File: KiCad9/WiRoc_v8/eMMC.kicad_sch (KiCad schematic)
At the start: 10 parts, among them U14 KLM8G1WEPD-B031

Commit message: etc
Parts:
- C33, C34, C86: LCSC Part # (none) -> C52923; Manufacturer (none) -> Samsung Electro-Mechanics; ManufacturerPartNumber (none) -> CL05A105KA5NQNC
- R26: LCSC Part # (none) -> C25804; Manufacturer (none) -> Uniroyal Elec; ManufacturerPartNumber (none) -> 0603WAF1002T5E
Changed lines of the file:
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@@
 			)
 		)
-		(property "Datasheet" "~"
+		(property "Datasheet" "https://jlcpcb.com/api/file/downloadByFileSystemAccessId/8579707174974914560"
 			(at 213.36 78.74 0)
 			(effects
@@
 		)
 		(property "Description" ""
+			(at 213.36 78.74 0)
+			(effects
+				(font
+					(size 1.27 1.27)
+				)
+				(hide yes)
+			)
+		)
+		(property "LCSC Part #" "C52923"
+			(at 213.36 78.74 0)
+			(effects
+				(font
+					(size 1.27 1.27)
+				)
+				(hide yes)
+			)
+		)
+		(property "Manufacturer" "Samsung Electro-Mechanics"
+			(at 213.36 78.74 0)
+			(effects
+				(font
+					(size 1.27 1.27)
+				)
+				(hide yes)
+			)
+		)
+		(property "ManufacturerPartNumber" "CL05A105KA5NQNC"
 			(at 213.36 78.74 0)
 			(effects
@@
 			)
 		)
-		(property "Datasheet" "~"
+		(property "Datasheet" "https://jlcpcb.com/api/file/downloadByFileSystemAccessId/8579707174974914560"
 			(at 36.83 153.67 0)
 			(effects
@@
 		)
 		(property "Description" ""
+			(at 36.83 153.67 0)
+			(effects
+				(font
+					(size 1.27 1.27)
+				)
+				(hide yes)
+			)
+		)
+		(property "LCSC Part #" "C52923"
+			(at 36.83 153.67 0)
+			(effects
+				(font
+					(size 1.27 1.27)
+				)
+				(hide yes)
+			)
+		)
+		(property "Manufacturer" "Samsung Electro-Mechanics"
+			(at 36.83 153.67 0)
+			(effects
+				(font
+					(size 1.27 1.27)
+				)
+				(hide yes)
+			)
+		)
+		(property "ManufacturerPartNumber" "CL05A105KA5NQNC"
 			(at 36.83 153.67 0)
 			(effects
@@
 			)
 		)
-		(property "Datasheet" "~"
+		(property "Datasheet" "https://jlcpcb.com/api/file/downloadByFileSystemAccessId/8579707174974914560"
 			(at 213.36 54.61 0)
 			(effects
@@
 		)
 		(property "Description" ""
+			(at 213.36 54.61 0)
+			(effects
+				(font
+					(size 1.27 1.27)
+				)
+				(hide yes)
+			)
+		)
+		(property "LCSC Part #" "C52923"
+			(at 213.36 54.61 0)
+			(effects
+				(font
+					(size 1.27 1.27)
+				)
+				(hide yes)
+			)
+		)
+		(property "Manufacturer" "Samsung Electro-Mechanics"
+			(at 213.36 54.61 0)
+			(effects
+				(font
+					(size 1.27 1.27)
+				)
+				(hide yes)
+			)
+		)
+		(property "ManufacturerPartNumber" "CL05A105KA5NQNC"
 			(at 213.36 54.61 0)
 			(effects
@@
 			(at 39.37 45.72 0)
 			(effects
+				(font
+					(size 1.27 1.27)
+				)
+				(hide yes)
+			)
+		)
+		(property "LCSC Part #" "C25804"
+			(at 39.37 45.72 0)
+			(effects
+				(font
+					(size 1.27 1.27)
+				)
+				(hide yes)
+			)
+		)
+		(property "Manufacturer" "Uniroyal Elec"
+			(at 39.37 45.72 0)
+			(effects
+				(font
+					(size 1.27 1.27)
+				)
+				(hide yes)
+			)
+		)
+		(property "ManufacturerPartNumber" "0603WAF1002T5E"
+			(at 39.37 45.72 0)
+			(effects

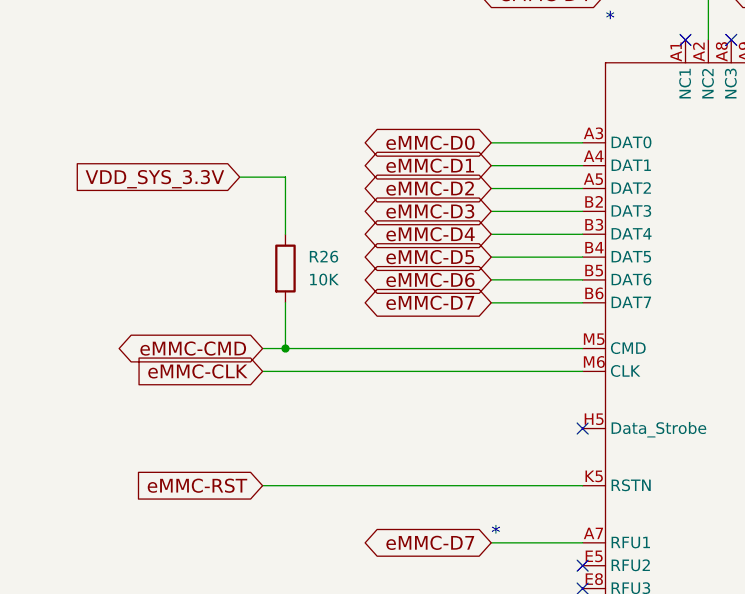
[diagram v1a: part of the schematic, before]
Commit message: more routing of WiRoc_v8, upgraded USBConnectorPlate to v9 and with ferrit beads, added an ESPHosted testboard
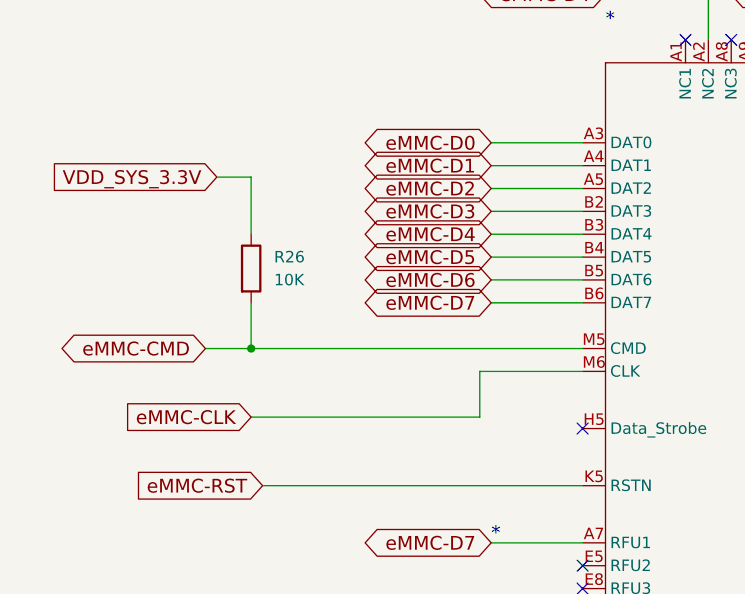
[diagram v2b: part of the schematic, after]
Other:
- moved on the sheet: R26
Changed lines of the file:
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@@
 	)
 	(junction
+		(at 35.56 54.61)
+		(diameter 0)
+		(color 0 0 0 0)
+	)
+	(junction
 		(at 66.04 176.53)
 		(diameter 0)
@@
 	)
 	(junction
-		(at 39.37 54.61)
-		(diameter 0)
-		(color 0 0 0 0)
-	)
-	(junction
 		(at 66.04 168.91)
 		(diameter 0)
@@
 	(wire
 		(pts
-			(xy 59.69 146.05) (xy 72.39 146.05)
+			(xy 60.96 57.15) (xy 72.39 57.15)
 		)
 		(stroke
@@
 	(wire
 		(pts
-			(xy 39.37 54.61) (xy 72.39 54.61)
+			(xy 59.69 146.05) (xy 72.39 146.05)
 		)
 		(stroke
@@
 	(wire
 		(pts
-			(xy 39.37 49.53) (xy 39.37 54.61)
+			(xy 35.56 49.53) (xy 35.56 54.61)
 		)
 		(stroke
@@
 	(wire
 		(pts
-			(xy 34.29 35.56) (xy 39.37 35.56)
+			(xy 31.75 35.56) (xy 35.56 35.56)
 		)
 		(stroke
@@
 	(wire
 		(pts
-			(xy 36.83 57.15) (xy 72.39 57.15)
+			(xy 35.56 62.23) (xy 60.96 62.23)
 		)
 		(stroke
@@
 	(wire
 		(pts
-			(xy 39.37 35.56) (xy 39.37 41.91)
+			(xy 35.56 35.56) (xy 35.56 41.91)
 		)
 		(stroke
@@
 	(wire
 		(pts
-			(xy 36.83 54.61) (xy 39.37 54.61)
+			(xy 30.48 54.61) (xy 35.56 54.61)
 		)
 		(stroke
@@
 	(wire
 		(pts
+			(xy 60.96 62.23) (xy 60.96 57.15)
+		)
+		(stroke
+			(width 0)
+			(type default)
+		)
+	)
+	(wire
+		(pts
 			(xy 63.5 134.62) (xy 72.39 134.62)
 		)
@@
 	(wire
 		(pts
+			(xy 35.56 54.61) (xy 72.39 54.61)
+		)
+		(stroke
+			(width 0)
+			(type default)
+		)
+	)
+	(wire
+		(pts
 			(xy 36.83 149.86) (xy 36.83 146.05)
 		)
@@
 	(global_label "eMMC-CMD"
 		(shape bidirectional)
-		(at 36.83 54.61 180)
+		(at 30.48 54.61 180)
 		(fields_autoplaced yes)
 		(effects
@@
 		)
 		(property "Intersheetrefs" "${INTERSHEET_REFS}"
-			(at 19.8999 54.61 0)
+			(at 13.5499 54.61 0)
 			(effects
 				(font
@@
 	(global_label "eMMC-CLK"
 		(shape input)
-		(at 36.83 57.15 180)
+		(at 35.56 62.23 180)
 		(fields_autoplaced yes)
 		(effects
@@
 		)
 		(property "Intersheetrefs" "${INTERSHEET_REFS}"
-			(at 21.5509 57.15 0)
+			(at 20.2809 62.23 0)
 			(effects
 				(font
@@
 	(global_label "VDD_SYS_3.3V"
 		(shape input)
-		(at 34.29 35.56 180)
+		(at 31.75 35.56 180)
 		(fields_autoplaced yes)
 		(effects
@@
 		)
 		(property "Intersheetrefs" "${INTERSHEET_REFS}"
-			(at 15.6728 35.56 0)
+			(at 13.1328 35.56 0)
 			(effects
 				(font
@@
 		)
 	)
+	(rule_area
+		(polyline
+			(pts
+				(xy 68.58 30.48) (xy 64.77 30.48) (xy 64.77 50.8) (xy 68.58 50.8)
+			)
+			(stroke
+				(width 0)
+				(type dash)
+			)
+			(fill
+				(type none)
+			)
+		)
+	)
+	(netclass_flag ""
+		(length 2.54)
+		(shape round)
+		(at 40.64 54.61 0)
+		(fields_autoplaced yes)
+		(effects
+			(font
+				(size 1.524 1.524)
+			)
+			(justify left bottom)
+		)
+		(property "Netclass" "eMMC-Cmd"
+			(at 41.2699 52.07 0)
+			(effects
+				(font
+					(size 1.27 1.27)
+				)
+				(justify left)
+			)
+		)
+		(property "Component Class" ""
+			(at -121.92 12.7 0)
+			(effects
+				(font
+					(size 1.27 1.27)
+					(italic yes)
+				)
+			)
+		)
+	)
+	(netclass_flag ""
+		(length 2.54)
+		(shape round)
+		(at 66.04 30.48 0)
+		(fields_autoplaced yes)
+		(effects
+			(font
+				(size 1.524 1.524)
+			)
+			(justify left bottom)
+		)
+		(property "Netclass" "eMMC-Data"
+			(at 66.6699 27.94 0)
+			(effects
+				(font
+					(size 1.27 1.27)
+				)
+				(justify left)
+			)
+		)
+		(property "Component Class" ""
+			(at -96.52 -11.43 0)
+			(effects
+				(font
+					(size 1.27 1.27)
+					(italic yes)
+				)
+			)
+		)
+	)
+	(netclass_flag ""
+		(length 2.54)
+		(shape round)
+		(at 45.72 62.23 0)
+		(effects
+			(font
+				(size 1.524 1.524)
+			)
+			(justify left bottom)
+		)
+		(property "Netclass" "eMMC-Clk"
+			(at 47.752 60.198 0)
+			(effects
+				(font
+					(size 1.27 1.27)
+				)
+				(justify left)
+			)
+		)
+		(property "Component Class" ""
+			(at -116.84 20.32 0)
+			(effects
+				(font
+					(size 1.27 1.27)
+					(italic yes)
+				)
+			)
+		)
+	)
 	(symbol
 		(lib_id "power:GND")
@@
 	(symbol
 		(lib_id "Device:R")
-		(at 39.37 45.72 0)
+		(at 35.56 45.72 0)
 		(unit 1)
 		(exclude_from_sim no)
@@
 		(fields_autoplaced yes)
 		(property "Reference" "R26"
-			(at 41.91 44.45 0)
+			(at 38.1 44.45 0)
 			(effects
 				(font
@@
 		)
 		(property "Value" "10K"
-			(at 41.91 46.99 0)
+			(at 38.1 46.99 0)
 			(effects
 				(font
@@
 		)
 		(property "Footprint" "Resistor_SMD:R_0402_1005Metric"
-			(at 37.592 45.72 90)
+			(at 33.782 45.72 90)
 			(effects
 				(font
@@
 		)
 		(property "Datasheet" "~"
-			(at 39.37 45.72 0)
+			(at 35.56 45.72 0)
 			(effects
 				(font
@@
 		)
 		(property "Description" ""
-			(at 39.37 45.72 0)
+			(at 35.56 45.72 0)
 			(effects
 				(font
@@
 		)
 		(property "LCSC Part #" "C25804"
-			(at 39.37 45.72 0)
+			(at 35.56 45.72 0)
 			(effects
 				(font
@@
 		)
 		(property "Manufacturer" "Uniroyal Elec"
-			(at 39.37 45.72 0)
+			(at 35.56 45.72 0)
 			(effects
 				(font
@@
 		)
 		(property "ManufacturerPartNumber" "0603WAF1002T5E"
-			(at 39.37 45.72 0)
+			(at 35.56 45.72 0)
 			(effects
 				(font

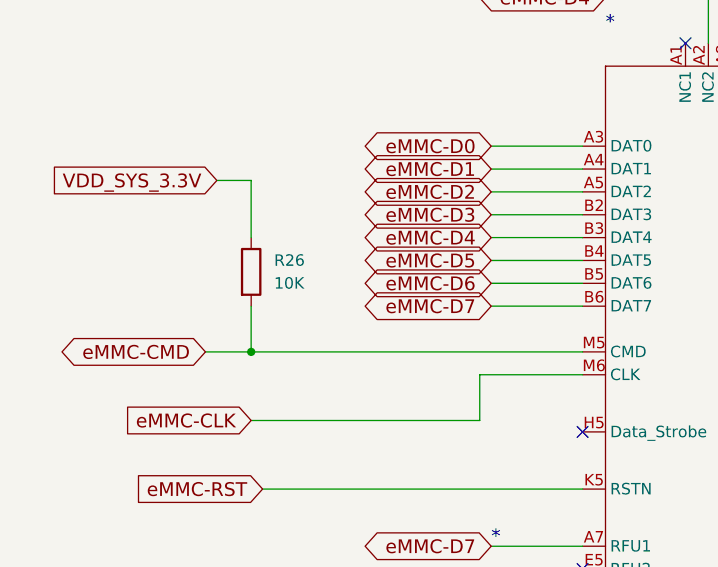
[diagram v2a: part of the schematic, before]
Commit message: add bom
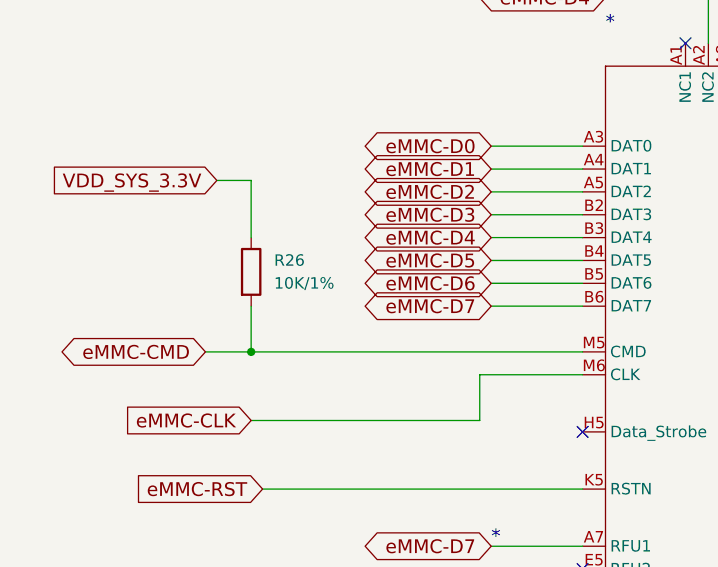
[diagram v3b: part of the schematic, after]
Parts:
- C32, C35, C80, C87, C88: IncludeInBOM (none) -> TRUE; JLCBasicExtended (none) -> Basic; LCSC Part # (none) -> C1525; Manufacturer (none) -> Samsung Electro-Mechanics; ManufacturerPartNumber (none) -> CL05B104KO5NNNC; Package (none) -> 0402
- C33, C34, C86: IncludeInBOM (none) -> TRUE; JLCBasicExtended (none) -> Basic; Package (none) -> 0402
- R26: value 10K -> 10K/1%; IncludeInBOM (none) -> TRUE; JLCBasicExtended (none) -> Basic; LCSC Part # C25804 -> C25744; ManufacturerPartNumber 0603WAF1002T5E -> 0402WGF1002TCE; Package (none) -> 0402
- U14: IncludeInBOM (none) -> TRUE; JLCBasicExtended (none) -> Extended; LCSC Part # (none) -> C2874142; Manufacturer (none) -> Samsung; ManufacturerPartNumber (none) -> KLM8G1WEPD-B031; Package (none) -> BGA-153

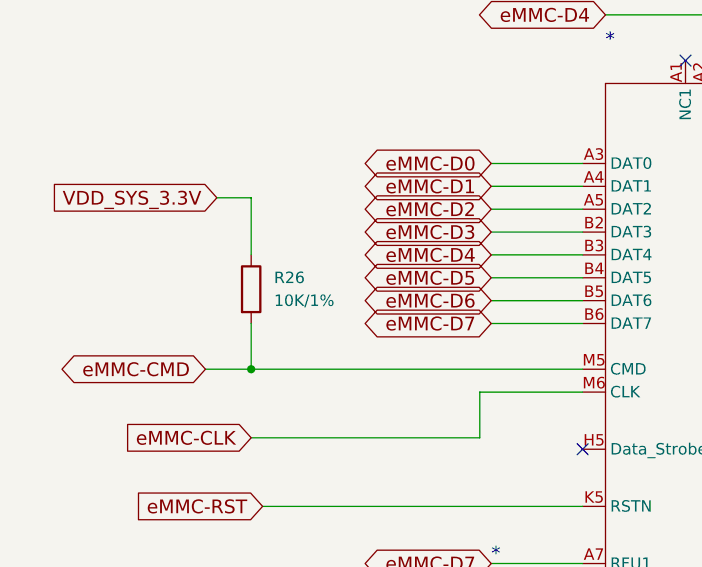
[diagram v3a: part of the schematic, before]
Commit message: adjustments length and width of traces
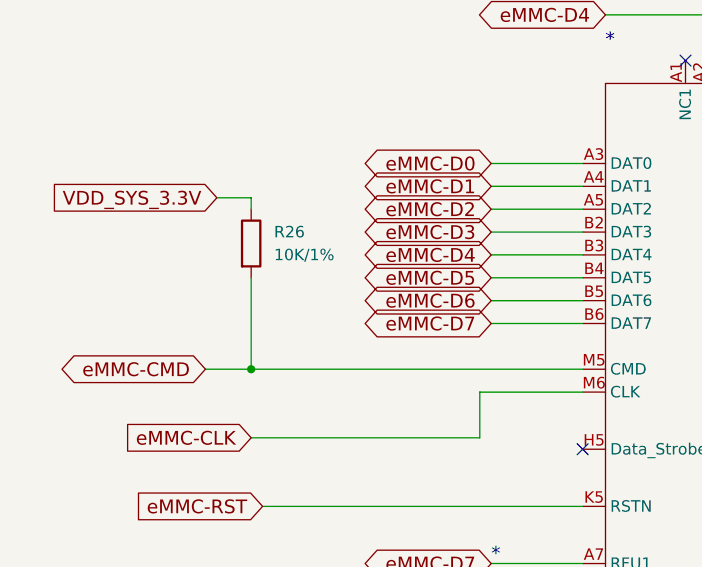
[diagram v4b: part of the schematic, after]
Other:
- moved on the sheet: R26
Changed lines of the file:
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@@
 	(wire
 		(pts
-			(xy 35.56 49.53) (xy 35.56 54.61)
+			(xy 35.56 44.45) (xy 35.56 54.61)
 		)
 		(stroke
@@
 	(wire
 		(pts
-			(xy 35.56 35.56) (xy 35.56 41.91)
+			(xy 35.56 35.56) (xy 35.56 36.83)
 		)
 		(stroke
@@
 	(symbol
 		(lib_id "Device:R")
-		(at 35.56 45.72 0)
+		(at 35.56 40.64 0)
 		(unit 1)
 		(exclude_from_sim no)
@@
 		(fields_autoplaced yes)
 		(property "Reference" "R26"
-			(at 38.1 44.45 0)
+			(at 38.1 39.37 0)
 			(effects
 				(font
@@
 		)
 		(property "Value" "10K/1%"
-			(at 38.1 46.99 0)
+			(at 38.1 41.91 0)
 			(effects
 				(font
@@
 		)
 		(property "Footprint" "Resistor_SMD:R_0402_1005Metric"
-			(at 33.782 45.72 90)
+			(at 33.782 40.64 90)
 			(effects
 				(font
@@
 		)
 		(property "Datasheet" "~"
-			(at 35.56 45.72 0)
+			(at 35.56 40.64 0)
 			(effects
 				(font
@@
 		)
 		(property "Description" ""
-			(at 35.56 45.72 0)
+			(at 35.56 40.64 0)
 			(effects
 				(font
@@
 		)
 		(property "LCSC Part #" "C25744"
-			(at 35.56 45.72 0)
+			(at 35.56 40.64 0)
 			(effects
 				(font
@@
 		)
 		(property "Manufacturer" "Uniroyal Elec"
-			(at 35.56 45.72 0)
+			(at 35.56 40.64 0)
 			(effects
 				(font
@@
 		)
 		(property "ManufacturerPartNumber" "0402WGF1002TCE"
-			(at 35.56 45.72 0)
+			(at 35.56 40.64 0)
 			(effects
 				(font
@@
 		)
 		(property "JLCBasicExtended" "Basic"
-			(at 35.56 45.72 0)
+			(at 35.56 40.64 0)
 			(effects
 				(font
@@
 		)
 		(property "Package" "0402"
-			(at 35.56 45.72 0)
+			(at 35.56 40.64 0)
 			(effects
 				(font
@@
 		)
 		(property "IncludeInBOM" "TRUE"
-			(at 35.56 45.72 0)
+			(at 35.56 40.64 0)
 			(effects
 				(font

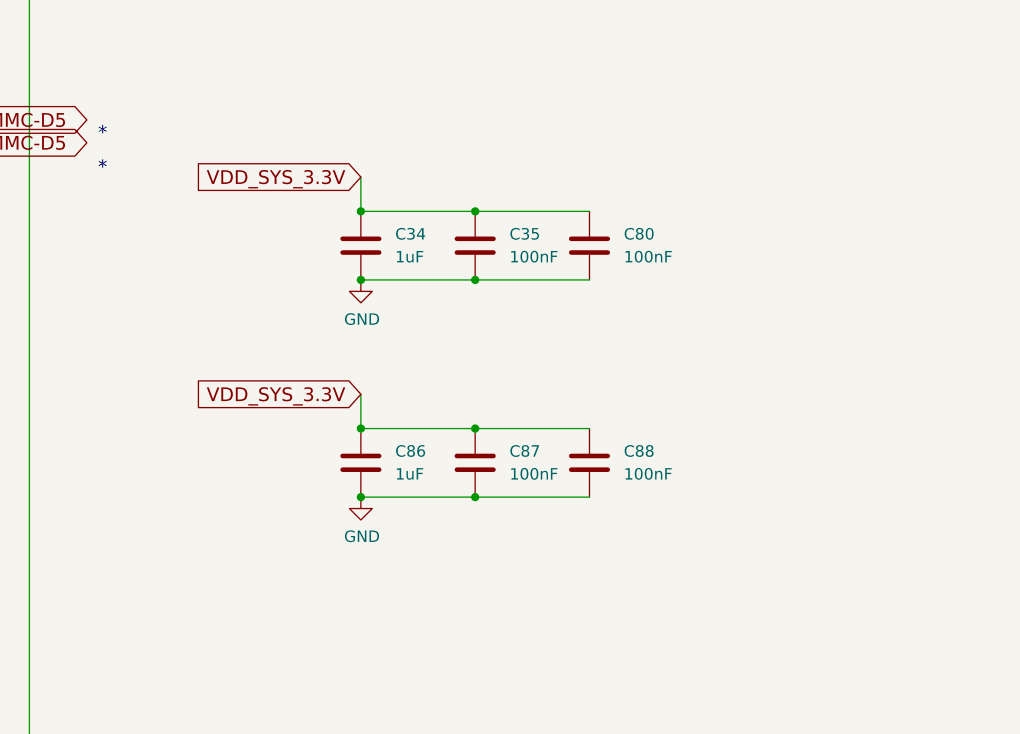
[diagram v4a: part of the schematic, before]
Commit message: change to 10uF in pdn, vdd-dram area to south caps, remove varistor, etc
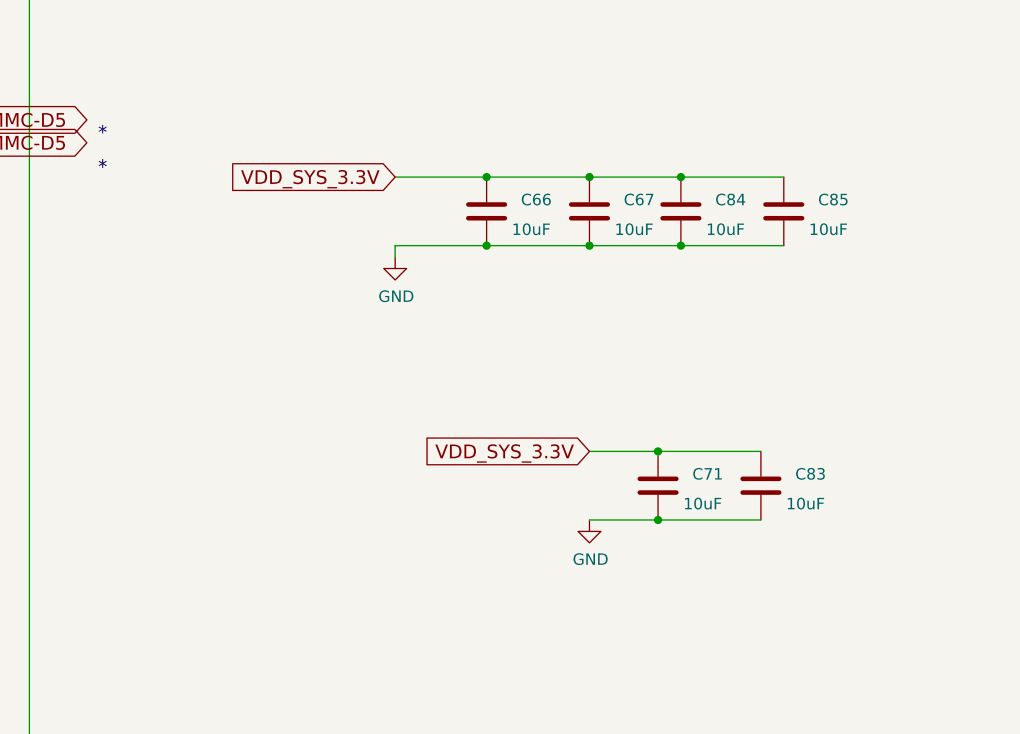
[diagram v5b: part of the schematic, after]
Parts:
- removed C34, C86: 1uF, Capacitor_SMD:C_0402_1005Metric, symbol Device:C
- removed C35, C80, C87, C88: 100nF, Capacitor_SMD:C_0402_1005Metric, symbol Device:C
- added C66, C67, C71, C83, C84, C85: 10uF, Capacitor_SMD:C_0402_1005Metric, symbol Device:C
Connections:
- net GND: now also C66.2, C67.2, C71.2, C83.2, C84.2, C85.2
- net VDD_SYS_3.3V: now also C66.1, C67.1, C71.1, C83.1, C84.1, C85.1
